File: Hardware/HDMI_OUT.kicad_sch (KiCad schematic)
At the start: 0 parts

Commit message: 增加基础的STM32代码
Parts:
- added U14: ~, persional_library:WFQFN-42_L9.0-W3.5-P0.50-BL-EP, symbol persional_library:IC_TS3DV642A0RUAR
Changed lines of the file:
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@@
 	(generator_version "8.0")
 	(paper "A4")
+	(symbol
+		(lib_id "persional_library:IC_TS3DV642A0RUAR")
+		(at 143.51 88.9 0)
+		(unit 1)
+		(exclude_from_sim no)
+		(in_bom yes)
+		(on_board yes)
+		(dnp no)
+		(fields_autoplaced yes)
+		(property "Reference" "U14"
+			(at 148.2642 119.38 0)
+			(effects
+				(font
+					(size 1.27 1.27)
+				)
+				(justify left)
+			)
+		)
+		(property "Value" "~"
+			(at 148.2642 120.65 0)
+			(effects
+				(font
+					(size 1.27 1.27)
+				)
+				(justify left)
+			)
+		)
+		(property "Footprint" "persional_library:WFQFN-42_L9.0-W3.5-P0.50-BL-EP"
+			(at 143.51 88.9 0)
+			(effects
+				(font
+					(size 1.27 1.27)
+				)
+				(hide yes)
+			)
+		)
+		(property "Datasheet" "https://www.ti.com/cn/lit/gpn/ts3dv642"
+			(at 143.51 88.9 0)
+			(effects
+				(font
+					(size 1.27 1.27)
+				)
+				(hide yes)
+			)
+		)
+		(property "Description" "开关电路:单刀双掷(SPDT);通道数:12;导通电阻(Ron@VCC):9.5Ω;"
+			(at 143.51 88.9 0)
+			(effects
+				(font
+					(size 1.27 1.27)
+				)
+				(hide yes)
+			)
+		)
+		(property "Manufacturer Part" "TS3DV642A0RUAR"
+			(at 143.51 88.9 0)
+			(effects
+				(font
+					(size 1.27 1.27)
+				)
+				(hide yes)
+			)
+		)
+		(property "Manufacturer" "TI(德州仪器)"
+			(at 143.51 88.9 0)
+			(effects
+				(font
+					(size 1.27 1.27)
+				)
+				(hide yes)
+			)
+		)
+		(property "Supplier Part" "C157482"
+			(at 143.51 88.9 0)
+			(effects
+				(font
+					(size 1.27 1.27)
+				)
+				(hide yes)
+			)
+		)
+		(property "Supplier" "LCSC"
+			(at 143.51 88.9 0)
+			(effects
+				(font
+					(size 1.27 1.27)
+				)
+				(hide yes)
+			)
+		)
+		(property "LCSC Part Name" "具有1.8V兼容控制和断电模式的12通道1:2多路复用器/多路解复用器"
+			(at 143.51 88.9 0)
+			(effects
+				(font
+					(size 1.27 1.27)
+				)
+				(hide yes)
+			)
+		)
+		(pin "40"
+		)
+		(pin "13"
+		)
+		(pin "14"
+		)
+		(pin "17"
+		)
+		(pin "28"
+		)
+		(pin "29"
+		)
+		(pin "31"
+		)
+		(pin "6"
+		)
+		(pin "1"
+		)
+		(pin "20"
+		)
+		(pin "22"
+		)
+		(pin "21"
+		)
+		(pin "12"
+		)
+		(pin "24"
+		)
+		(pin "23"
+		)
+		(pin "26"
+		)
+		(pin "19"
+		)
+		(pin "27"
+		)
+		(pin "30"
+		)
+		(pin "32"
+		)
+		(pin "3"
+		)
+		(pin "10"
+		)
+		(pin "36"
+		)
+		(pin "37"
+		)
+		(pin "4"
+		)
+		(pin "41"
+		)
+		(pin "11"
+		)
+		(pin "33"
+		)
+		(pin "39"
+		)
+		(pin "16"
+		)
+		(pin "42"
+		)
+		(pin "43"
+		)
+		(pin "15"
+		)
+		(pin "34"
+		)
+		(pin "38"
+		)
+		(pin "7"
+		)
+		(pin "25"
+		)
+		(pin "35"
+		)
+		(pin "8"
+		)
+		(pin "9"
+		)
+		(pin "5"
+		)
+		(pin "18"
+		)
+		(pin "2"
+		)
+		(instances
+			(project ""
+				(path "/bb6002ed-6e0a-40ea-a48c-f92cae8db5fa/9319a559-c36b-4bac-ac3b-ca0b3de1b8e6"
+					(reference "U14")
+					(unit 1)
+				)
+			)
+		)
+	)
 )

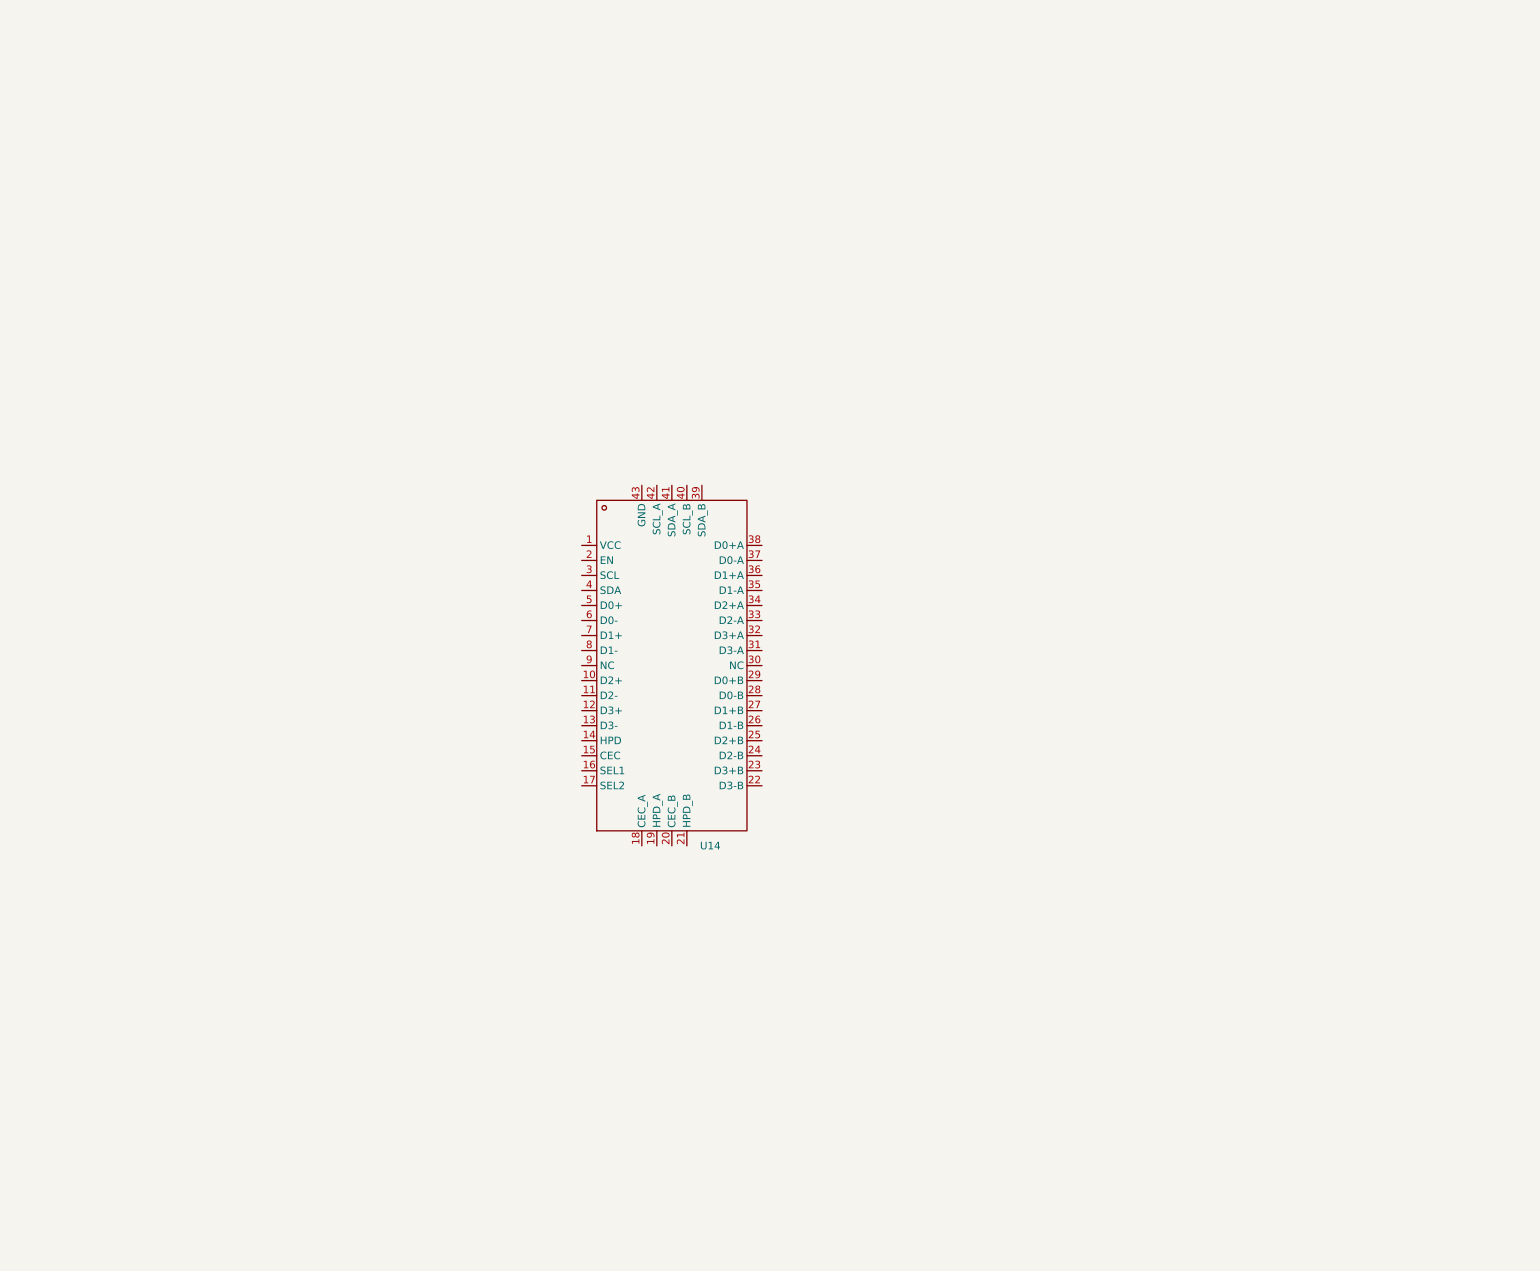
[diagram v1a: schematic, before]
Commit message: 完成除MCU外的设计
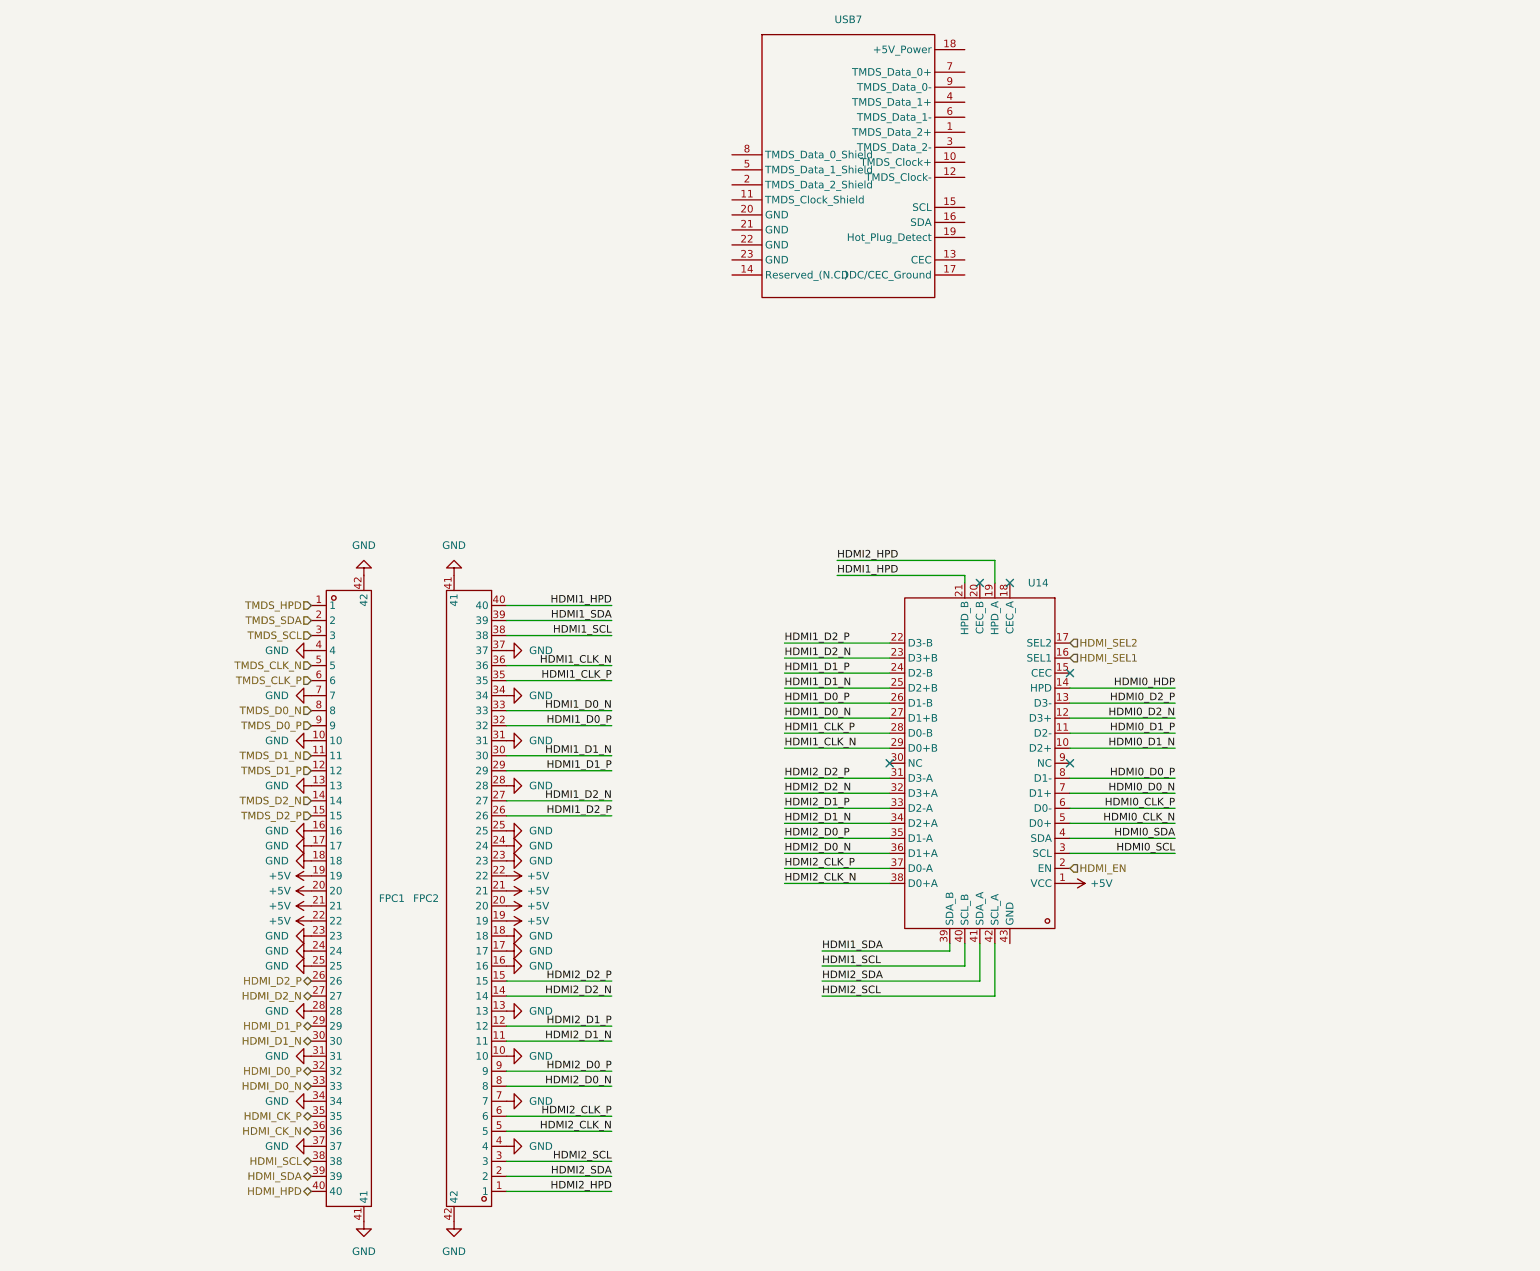
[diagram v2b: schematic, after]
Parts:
- added FPC1, FPC2: ~, persional_library:FPC-SMD_40P-P0.50_XUNPU_FPC-05FB-40PH20, symbol persional_library:Connect_FPC_40P
- added USB7: ~, persional_library:HDMI-SMD_HDMI-001S, symbol persional_library:Connect_HDMI_001S
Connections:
- net +5V: now reaches U14.1 (VCC)
- net +5V: now also FPC1.19, FPC1.20, FPC1.21, FPC1.22, FPC2.19, FPC2.20, FPC2.21, FPC2.22
- net HDMI0_D1_N: now reaches U14.10 (D2+)
- net HDMI0_D1_P: now reaches U14.11 (D2-)
- net HDMI0_D2_N: now reaches U14.12 (D3+)
- net HDMI0_D2_P: now reaches U14.13 (D3-)
- net HDMI0_HDP: now reaches U14.14 (HPD)
- net HDMI_SEL1: now reaches U14.16 (SEL1)
- net HDMI_SEL2: now reaches U14.17 (SEL2)
- net HDMI2_HPD: now reaches U14.19 (HPD_A)
- net HDMI2_HPD: now also FPC2.1
- net HDMI_EN: now reaches U14.2 (EN)
- net HDMI1_HPD: now reaches U14.21 (HPD_B)
- net HDMI1_HPD: now also FPC2.40
- net HDMI1_D2_P: now reaches U14.22 (D3-B)
- net HDMI1_D2_P: now also FPC2.26
- net HDMI1_D2_N: now reaches U14.23 (D3+B)
- net HDMI1_D2_N: now also FPC2.27
- net HDMI1_D1_P: now reaches U14.24 (D2-B)
- net HDMI1_D1_P: now also FPC2.29
- net HDMI1_D1_N: now reaches U14.25 (D2+B)
- net HDMI1_D1_N: now also FPC2.30
- net HDMI1_D0_P: now reaches U14.26 (D1-B)
- net HDMI1_D0_P: now also FPC2.32
- net HDMI1_D0_N: now reaches U14.27 (D1+B)
- net HDMI1_D0_N: now also FPC2.33
- net HDMI1_CLK_P: now reaches U14.28 (D0-B)
- net HDMI1_CLK_P: now also FPC2.35
- net HDMI1_CLK_N: now reaches U14.29 (D0+B)
- net HDMI1_CLK_N: now also FPC2.36
- net HDMI0_SCL: now reaches U14.3 (SCL)
- net HDMI2_D2_P: now reaches U14.31 (D3-A)
- net HDMI2_D2_P: now also FPC2.15
- net HDMI2_D2_N: now reaches U14.32 (D3+A)
- net HDMI2_D2_N: now also FPC2.14
- net HDMI2_D1_P: now reaches U14.33 (D2-A)
- net HDMI2_D1_P: now also FPC2.12
- net HDMI2_D1_N: now reaches U14.34 (D2+A)
- net HDMI2_D1_N: now also FPC2.11
- net HDMI2_D0_P: now reaches U14.35 (D1-A)
- net HDMI2_D0_P: now also FPC2.9
- net HDMI2_D0_N: now reaches U14.36 (D1+A)
- net HDMI2_D0_N: now also FPC2.8
- net HDMI2_CLK_P: now reaches U14.37 (D0-A)
- net HDMI2_CLK_P: now also FPC2.6
- net HDMI2_CLK_N: now reaches U14.38 (D0+A)
- net HDMI2_CLK_N: now also FPC2.5
- net HDMI1_SDA: now reaches U14.39 (SDA_B)
- net HDMI1_SDA: now also FPC2.39
- net HDMI0_SDA: now reaches U14.4 (SDA)
- net HDMI1_SCL: now reaches U14.40 (SCL_B)
- net HDMI1_SCL: now also FPC2.38
- net HDMI2_SDA: now reaches U14.41 (SDA_A)
- net HDMI2_SDA: now also FPC2.2
- net HDMI2_SCL: now reaches U14.42 (SCL_A)
- net HDMI2_SCL: now also FPC2.3
- net HDMI0_CLK_N: now reaches U14.5 (D0+)
- net HDMI0_CLK_P: now reaches U14.6 (D0-)
- net HDMI0_D0_N: now reaches U14.7 (D1+)
- net HDMI0_D0_P: now reaches U14.8 (D1-)
- new net GND: FPC1.10, FPC1.13, FPC1.16, FPC1.17, FPC1.18, FPC1.23, FPC1.24, FPC1.25, FPC1.28, FPC1.31, FPC1.34, FPC1.37, FPC1.4, FPC1.41, FPC1.42, FPC1.7, FPC2.10, FPC2.13, FPC2.16, FPC2.17, FPC2.18, FPC2.23, FPC2.24, FPC2.25, FPC2.28, FPC2.31, FPC2.34, FPC2.37, FPC2.4, FPC2.41, FPC2.42, FPC2.7
- new net HDMI_CK_N: FPC1.36
- new net HDMI_CK_P: FPC1.35
- new net HDMI_D0_N: FPC1.33
- new net HDMI_D0_P: FPC1.32
- new net HDMI_D1_N: FPC1.30
- new net HDMI_D1_P: FPC1.29
- new net HDMI_D2_N: FPC1.27
- new net HDMI_D2_P: FPC1.26
- new net HDMI_HPD: FPC1.40
- new net HDMI_SCL: FPC1.38
- new net HDMI_SDA: FPC1.39
- new net TMDS_CLK_N: FPC1.5
- new net TMDS_CLK_P: FPC1.6
- new net TMDS_D0_N: FPC1.8
- new net TMDS_D0_P: FPC1.9
- new net TMDS_D1_N: FPC1.11
- new net TMDS_D1_P: FPC1.12
- new net TMDS_D2_N: FPC1.14
- new net TMDS_D2_P: FPC1.15
- new net TMDS_HPD: FPC1.1
- new net TMDS_SCL: FPC1.3
- new net TMDS_SDA: FPC1.2
- no-connect marks 0 -> 5
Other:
- moved on the sheet: U14

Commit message: 修改了电源供电部分的内容
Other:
- moved on the sheet: FPC1, FPC2, U14, USB7

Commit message: complete sch
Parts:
- added C109: 100nF, persional_library:C0603, symbol persional_library:C0603
- added D8: ~, persional_library:SOD-323F_L1.7-W1.3-LS2.5-R-RD, symbol persional_library:Diode_1N4148WSL
- added R85, R86: 2.2kΩ, persional_library:R0603, symbol persional_library:R0603
- added R89: 100kΩ, persional_library:R0603, symbol persional_library:R0603
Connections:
- net +5V: now also USB7.18 (+5V_Power), D8.2; no longer U14.1 (VCC)
- net GND: now also USB7.11 (TMDS_Clock_Shield), USB7.14 (Reserved_(N.C.)), USB7.17 (DDC/CEC_Ground), USB7.2 (TMDS_Data_2_Shield), USB7.20 (GND), USB7.21 (GND), USB7.22 (GND), USB7.23 (GND), USB7.5 (TMDS_Data_1_Shield), USB7.8 (TMDS_Data_0_Shield), C109.2, R89.2
- net HDMI0_CLK_N: now also USB7.12 (TMDS_Clock-)
- net HDMI0_CLK_P: now also USB7.10 (TMDS_Clock+)
- net HDMI0_D0_N: now also USB7.9 (TMDS_Data_0-)
- net HDMI0_D0_P: now also USB7.7 (TMDS_Data_0+)
- net HDMI0_D1_N: now also USB7.6 (TMDS_Data_1-)
- net HDMI0_D1_P: now also USB7.4 (TMDS_Data_1+)
- net HDMI0_D2_N: now also USB7.3 (TMDS_Data_2-)
- net HDMI0_D2_P: now also USB7.1 (TMDS_Data_2+)
- net HDMI0_HDP: now also USB7.19 (Hot_Plug_Detect), R89.1
- net HDMI0_SCL: now also USB7.15 (SCL), R86.2
- net HDMI0_SDA: now also USB7.16 (SDA), R85.2
- new net: D8.1, R85.1, R86.1
- new net +3V3: C109.1, U14.1 (VCC)
- no-connect marks 5 -> 6
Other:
- moved on the sheet: USB7
